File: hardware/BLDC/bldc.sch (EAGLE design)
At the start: 29 parts, among them U1 MA702, U2 DRV8323RS, U3 TPN7R006PL, U4 TPN7R006PL, U5 TPN7R006PL, U6 TPN7R006PL, U7 TPN7R006PL, U8 TPN7R006PL, U9 STM32G4_UFQFPN48_T1

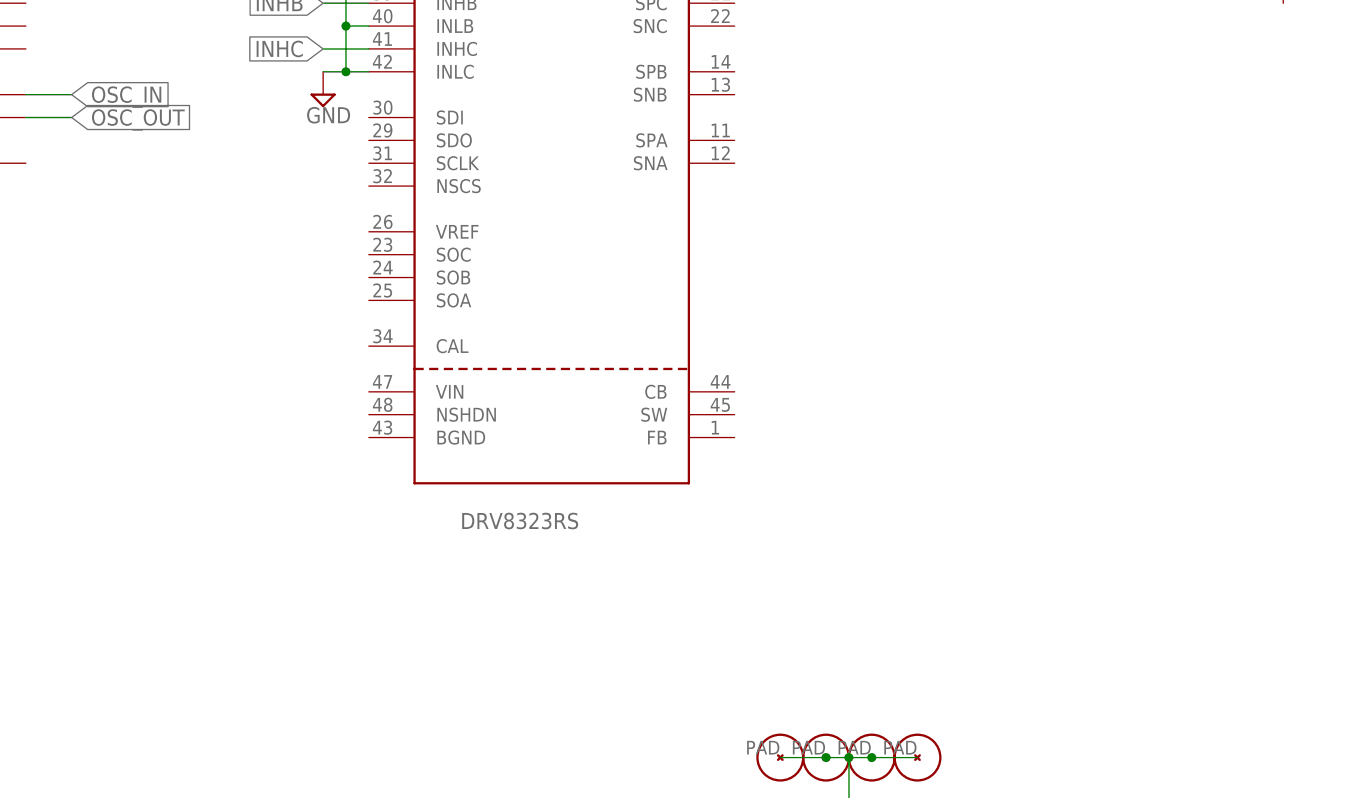
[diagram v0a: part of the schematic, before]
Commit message: Mostly updates to add inductor
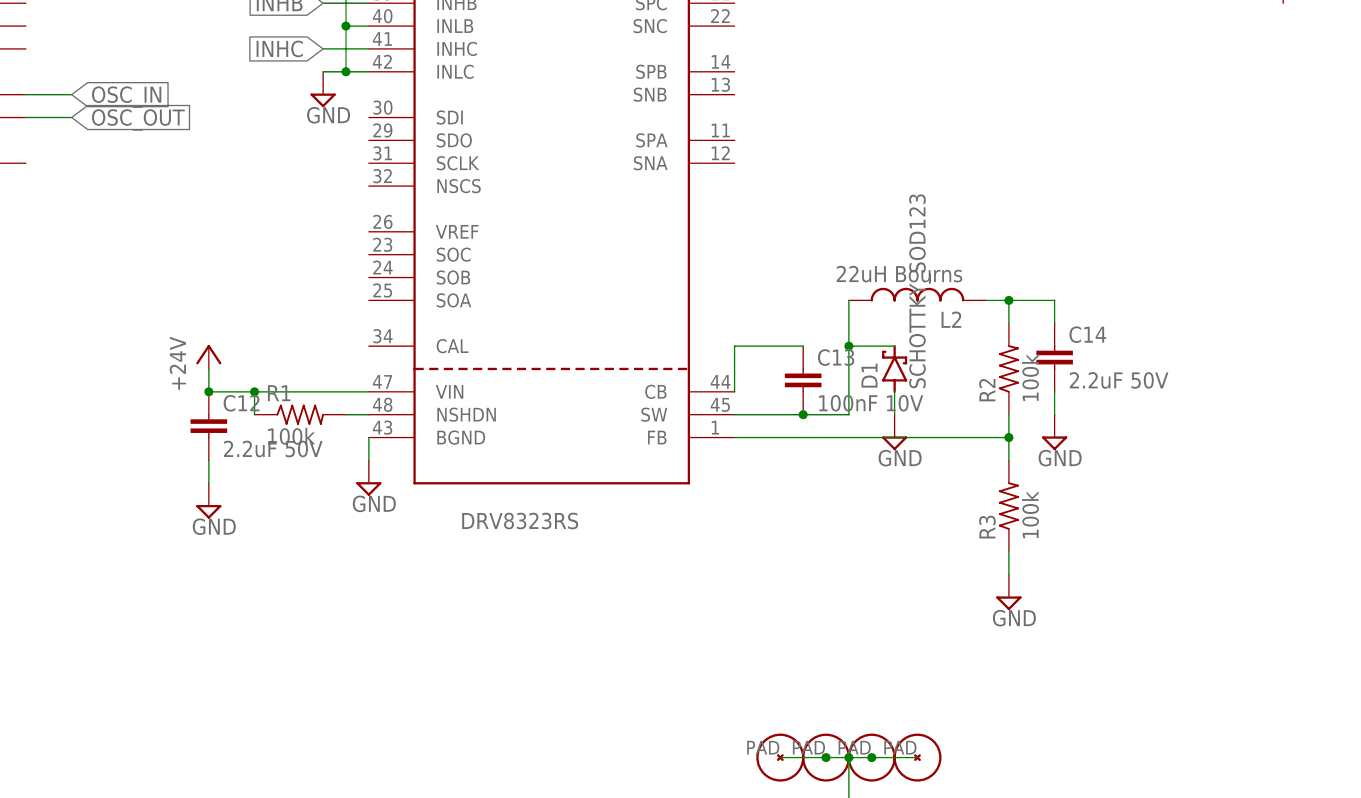
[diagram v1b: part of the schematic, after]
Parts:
- removed U$1: WIRE_HOLE_AWG_18, _T_conn:WIRE_HOLE_AWG_18
- added C12, C14: 2.2uF 50V, _T_rcl:C0603
- added C13: 100nF 10V, _T_rcl:C0603
- added D1: SCHOTTKY_SOD123, _T_rcl:SCHOTTKY_SOD123
- added L2: 22uH Bourns, _T_rcl:L_SDR0302
- added R1, R2, R3: 100k, _T_rcl:R0402
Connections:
- removed net GND: C1.2, C10.2, C11.2, C4.2, C5.2, C6.2, C7.2, C8.2, C9.2, H1.P1, H2.P1, H3.P1, H4.P1, U1.GND, U1.TEST, U2.INLA, U2.INLB, U2.INLC, U9B.EPAD
- new net N#8: C1.2, C10.2, C11.2, C12.2, C14.2, C4.2, C5.2, C6.2, C7.2, C8.2, C9.2, D1.A, H1.P1, H2.P1, H3.P1, H4.P1, R3.1, U1.GND, U1.TEST, U2.BGND, U2.INLA, U2.INLB, U2.INLC, U9B.EPAD
- new net N$10: C14.1, L2.2, R2.2
- new net N$5: R1.2, U2.NSHDN
- new net N$6: C13.1, U2.CB
- new net N$8: C13.2, D1.C, L2.1, U2.SW
- new net N$9: R2.1, R3.2, U2.FB
- net +3V3: now also C12.1, R1.1, U2.VIN

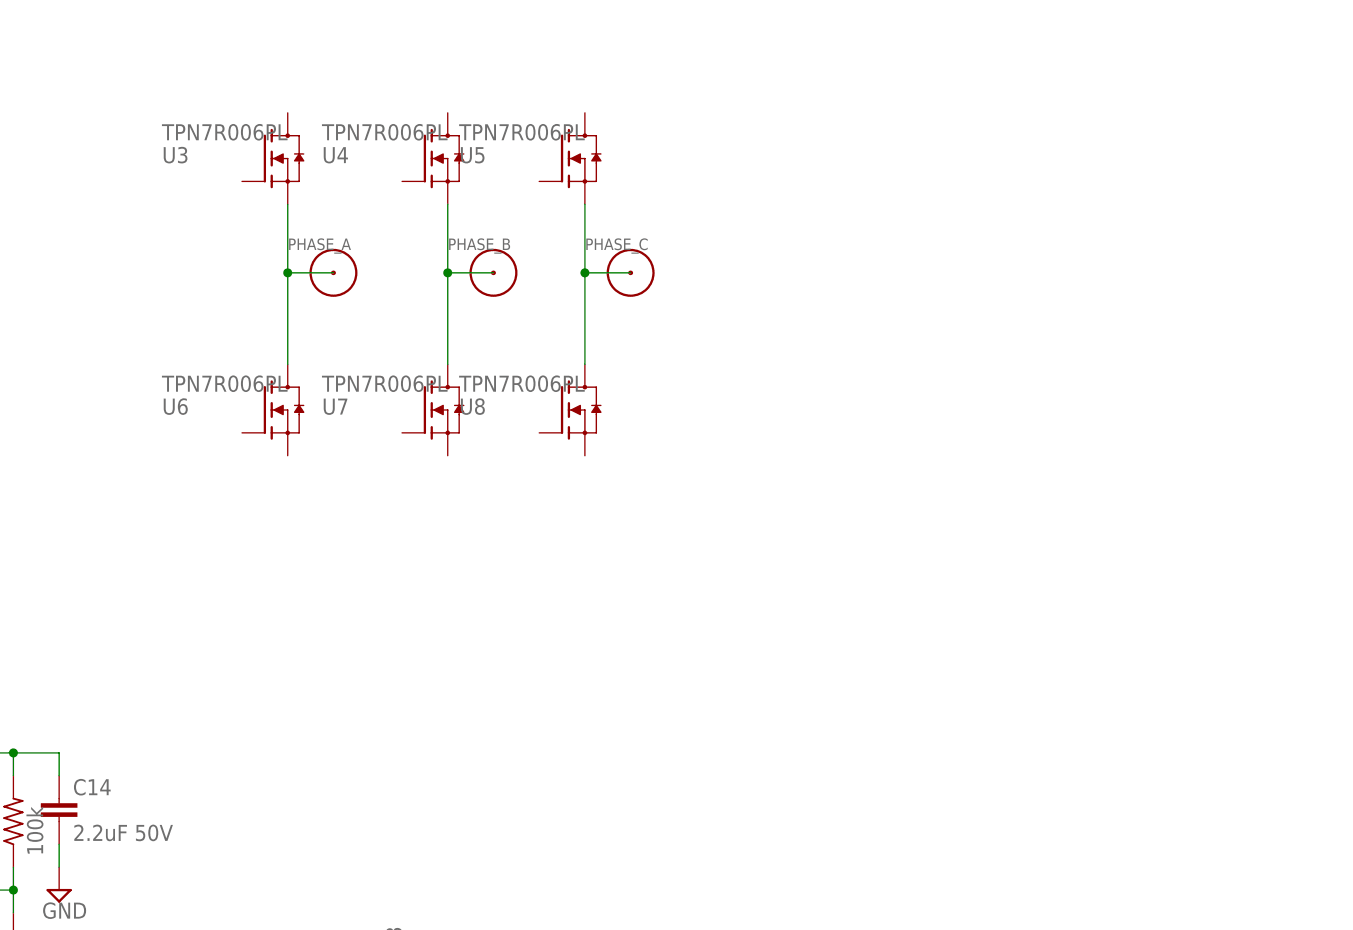
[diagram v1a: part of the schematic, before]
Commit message: Added xt30
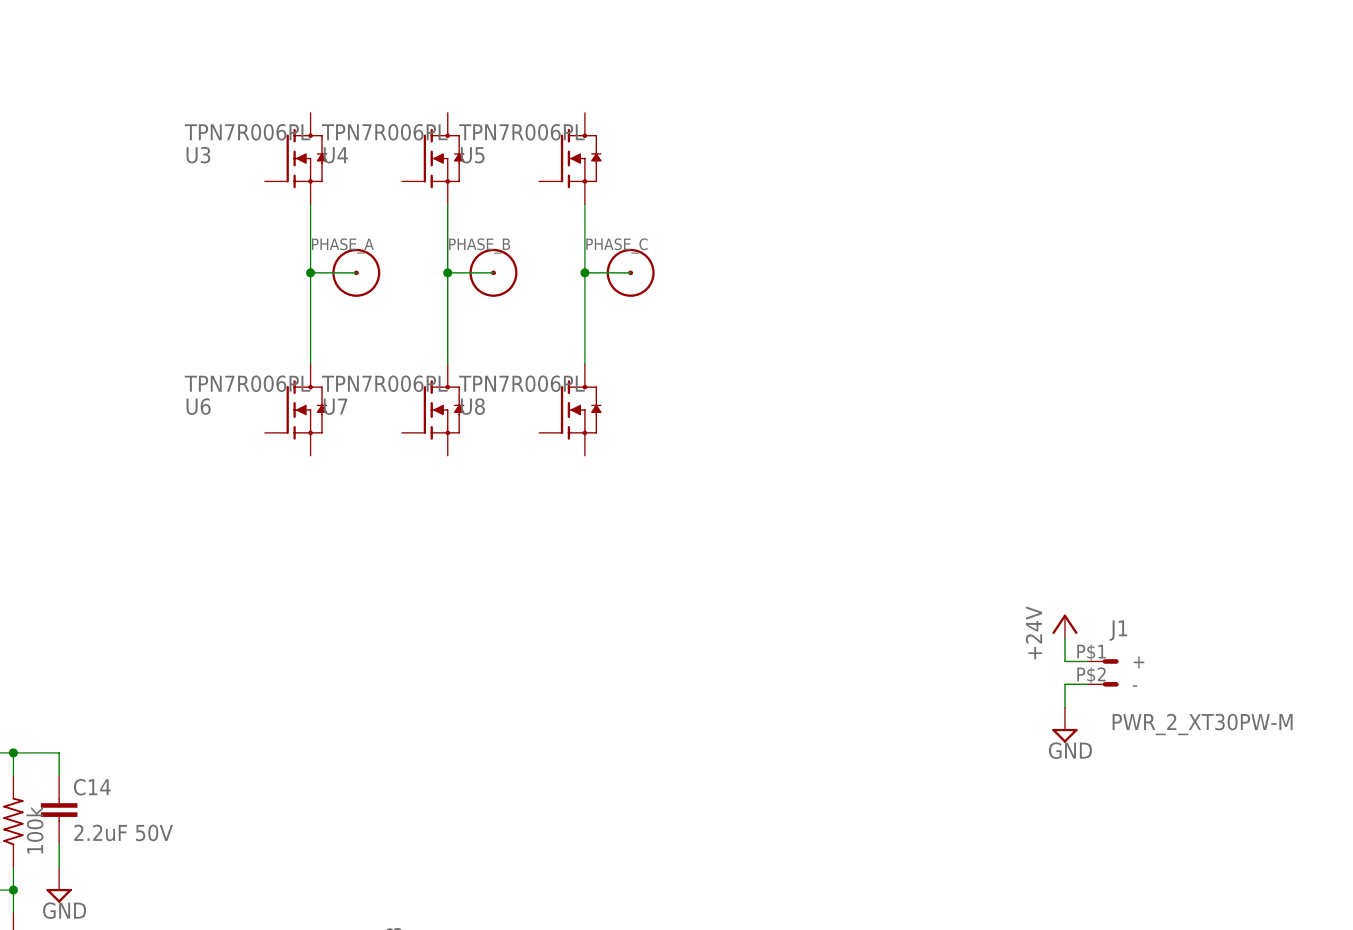
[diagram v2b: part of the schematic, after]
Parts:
- added J1: PWR_2_XT30PW-M, _T_conn:PWR_2_XT30PW-M
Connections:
- new net +24V: C12.1, J1.+, R1.1, U2.VIN
- new net GND: J1.-
- net +3V3: no longer C12.1, R1.1, U2.VIN
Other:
- moved on the sheet: PHASE_A, U3, U6

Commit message: Added bulk caps
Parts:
- added C15, C16, C17, C18, C19, C20, C21, C22, C23, C24, C25, C26, C27, C28, C29, C30: 10uF V50, _T_rcl:C1206
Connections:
- net +24V: now also C15.1, C16.1, C17.1, C18.1, C19.1, C20.1, C21.1, C22.1, C23.1, C24.1, C25.1, C26.1, C27.1, C28.1, C29.1, C30.1
- net GND: now also C15.2, C16.2, C17.2, C18.2, C19.2, C20.2, C21.2, C22.2, C23.2, C24.2, C25.2, C26.2, C27.2, C28.2, C29.2, C30.2

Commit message: Finishing up DRV8323RS
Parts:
- added C31, C32: 1uf 50v, _T_rcl:C0603
- added C33: 47nF 50v, _T_rcl:C0402
- added C34, C35: 1uf 10v, _T_rcl:C0603
- added J2: LINEAR_2_JST_SH_RA, _T_conn:LINEAR_2_JST_SH_RA
- added R4: 120, _T_rcl:R0402
- added U10: MCP2542FD, _T_ic:MCP2542FD
- C14: value 2.2uF 50V -> 2.2uF 10V
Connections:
- net N$2 renamed SHA
- net N$3 renamed SHB
- net N$4 renamed SHC
- new net 3.3V30MA: C34.1, U2.DVDD
- new net DRV_ENABLE: U2.ENABLE, U9A.PC6
- new net GHA: U3.G
- new net GHB: U4.G
- new net GHC: U5.G
- new net GLA: U6.G
- new net GLB: U7.G
- new net GLC: U8.G
- new net N$11: J2.P1, R4.2, U10.CANH
- new net N$12: J2.P2, R4.1, U10.CANL
- new net N$13: C31.2, U2.VCP
- new net N$14: C33.1, U2.CPH
- new net N$15: C33.2, U2.CPL
- new net N$16: U2.GLB
- new net N$17: U2.GLC
- new net N$18: U2.SPA
- new net N$19: U2.SPB
- new net N$2: U2.GHA
- new net N$20: U2.SPC
- new net N$3: U2.GHB
- new net N$4: U2.GHC
- new net SPA: U6.S
- new net SPB: U7.S
- new net SPC: U8.S
- new net VCC: C14.1, C35.1, L2.2, R2.2, U10.VDD, U2.VREF
- net +24V: now also C31.1, C32.1, U2.VM
- net DRV_CS: now also U2.NSCS
- net DRV_MISO: now also U2.SDO
- net DRV_MOSI: now also U2.SDI
- net DRV_SCK: now also U2.SCLK
- net GND: now also C32.2, C34.2, C35.2, U2.AGND, U2.DGND, U2.PGND
- net N$10: now also U2.GLA; no longer C14.1, L2.2, R2.2
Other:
- moved on the sheet: U9A

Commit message: Laying out board now
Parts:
- added C36, C41: 0.1uF 10V, _T_rcl:C0402
- added C37, C42: 6.8pF 10V, _T_rcl:C0402
- added C38: 1uF 10V, _T_rcl:C0402
- added C39, C40: 22uF 10V, _T_rcl:C0402
- added R10: 150k 1%, _T_rcl:R0402
- added R11: 10k 1%, _T_rcl:R0402
- added R5, R6, R7: 0.001, _T_rcl:R_SENSE_1210
- added R8, R9: 10k, _T_rcl:R0402
- added U11: LDFM33PUR, _T_ic:LDFM33PUR
- added X1: CRYSTAL_NX2016SA-24MHZ-EXS00A-CS11335, _T_ic:CRYSTAL_NX2016SA-24MHZ-EXS00A-CS11335
- renumbered C15 to GND
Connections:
- removed net N#8: C1.2, C10.2, C11.2, C12.2, C14.2, C4.2, C5.2, C6.2, C7.2, C8.2, C9.2, D1.A, H1.P1, H2.P1, H3.P1, H4.P1, R3.1, U1.GND, U1.TEST, U2.BGND, U2.INLA, U2.INLB, U2.INLC, U9B.EPAD
- removed net N$10: U2.GLA
- removed net N$16: U2.GLB
- removed net N$17: U2.GLC
- removed net N$18: U2.SPA
- removed net N$19: U2.SPB
- removed net N$20: U2.SPC
- removed net N$4: U2.GHC
- removed net N$7: C2.2, C3.2
- removed net OSC_IN: U9A.PF0-OSC_IN
- removed net OSC_OUT: U9A.PF1-OSC_OUT
- removed net VCC: C14.1, C35.1, L2.2, R2.2, U10.VDD, U2.VREF
- new net +5V: C14.1, C36.1, C38.1, L2.2, R2.2, U10.VDD, U11.EN, U11.VIN
- new net CAL: U2.CAL
- new net GNDNAME: C1.2, C10.2, C11.2, C12.2, C14.2, C5.2, C6.2, C7.2, C8.2, C9.2, D1.A, R3.1, U1.GND, U1.TEST, U2.BGND, U2.INLA, U2.INLB, U2.INLC
- new net N$21: R7.1, U8.S
- new net N$22: R6.1, U7.S
- new net N$23: R5.1, U6.S
- new net NFAULT: R8.1, U2.NFAULT
- new net NRST: U9A.PG10-NRST
- new net SENSE_A: U2.SOA, U9A.PA1
- new net SENSE_B: U2.SOB, U9A.PA0
- new net SENSE_C: U2.SOC, U9A.PB1
- new net SNA: R5.K2, U2.SNA
- new net SNB: R6.K2, U2.SNB
- new net SNC: R7.K2, U2.SNC
- new net VBUS_SENSE: R10.1, R11.2, U9A.PB12
- new net VDRAIN: U2.VDRAIN
- net +24V: now also C5.1, R10.2, U3.D, U4.D, U5.D, U9B.VBAT
- net +3V3: now also C35.1, C39.1, C40.1, C41.1, R8.2, R9.2, U10.VIO, U11.VOUT, U2.VREF; no longer C5.1, U9B.VBAT
- net DRV_CS: now also U9A.PB11; no longer U9A.PB12
- net DRV_MISO: now also R9.1
- net FDCAN1_RX: now also U10.RXD
- net FDCAN1_TX: now also U10.TXD
- net GHA: now also U2.GHA
- net GHB: now also U2.GHB
- net GHC: now also U2.GHC
- net GLA: now also U2.GLA
- net GLB: now also U2.GLB
- net GLC: now also U2.GLC
- net GND: now also C2.2, C3.2, C36.2, C37.2, C38.2, C39.2, C4.2, C40.2, C41.2, C42.2, H1.P1, H2.P1, H3.P1, H4.P1, R11.1, R5.2, R6.2, R7.2, U10.STBY, U10.VSS, U11.GND, U9B.EPAD, X1.GND
- net N$2: now also C37.1, U9A.PF0-OSC_IN, X1.2; no longer U2.GHA
- net N$3: now also C42.1, U9A.PF1-OSC_OUT, X1.1; no longer U2.GHB
- net SHA: now also U2.SHA
- net SHB: now also U2.SHB
- net SHC: now also U2.SHC
- net SPA: now also R5.K1, U2.SPA; no longer U6.S
- net SPB: now also R6.K1, U2.SPB; no longer U7.S
- net SPC: now also R7.K1, U2.SPC; no longer U8.S
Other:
- moved on the sheet: C10, C11, C2, C3, C4, C5, C6, C7, C8, C9, L1, PHASE_A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

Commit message: Reposition
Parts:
- added J3: LINEAR_8_JST_PH_RA, _T_conn:LINEAR_8_JST_PH_RA
- J2: value LINEAR_2_JST_SH_RA -> LINEAR_3_JST_PH_RA; device _T_conn:LINEAR_2_JST_SH_RA -> _T_conn:LINEAR_3_JST_PH_RA
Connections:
- removed net GNDNAME: C1.2, C10.2, C11.2, C12.2, C14.2, C5.2, C6.2, C7.2, C8.2, C9.2, D1.A, R3.1, U1.GND, U1.TEST, U2.BGND, U2.INLA, U2.INLB, U2.INLC
- net +24V: no longer C5.1, U9B.VBAT
- net +3V3: now also C5.1, J3.P1, U9B.VBAT
- net GND: now also C1.2, C10.2, C11.2, C12.2, C14.2, C5.2, C6.2, C7.2, C8.2, C9.2, D1.A, J2.P3, J3.P8, R3.1, U1.GND, U1.TEST, U2.BGND, U2.INLA, U2.INLB, U2.INLC
- net LPUART1_RX: now also J3.P7
- net LPUART1_TX: now also J3.P6
- net NRST: now also J3.P2
- net SWCLK: now also J3.P3
- net SWDIO: now also J3.P4
- net SWO: now also J3.P5
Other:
- moved on the sheet: C10, C11, C2, C3, C4, C5, C6, C7, C8, C9, L1, U9B

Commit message: V1 done
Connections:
- removed net VDRAIN: U2.VDRAIN
- net +24V: now also U2.VDRAIN
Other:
- moved on the sheet: D1
